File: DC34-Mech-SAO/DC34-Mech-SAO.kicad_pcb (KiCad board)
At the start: 2 copper layers, 27.9 x 38 mm, 20 parts, among them J1 Conn_01x06_Male, J2 Conn_01x03_Male, U1 ATtiny816-M

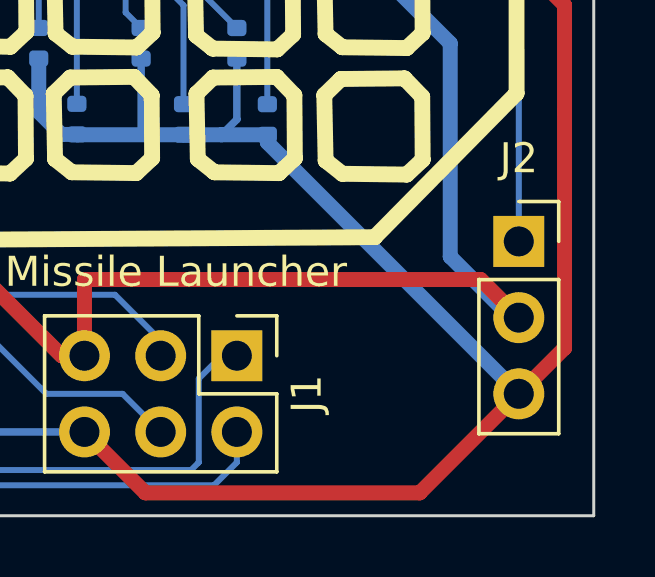
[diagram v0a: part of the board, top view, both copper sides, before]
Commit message: Added silkscreen.
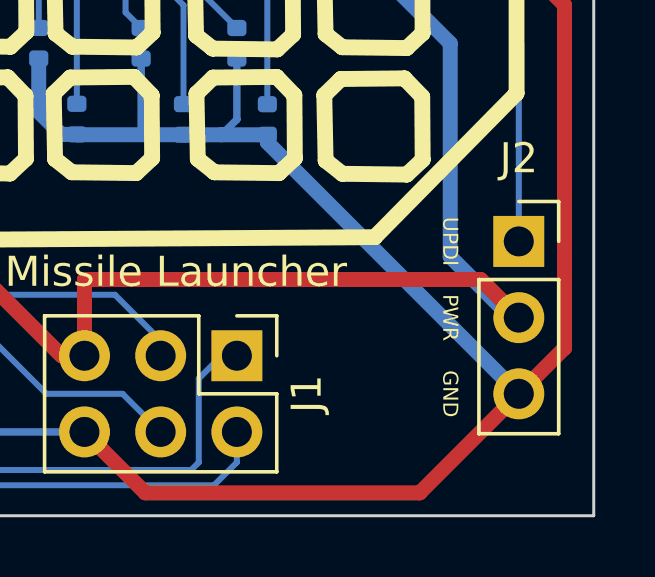
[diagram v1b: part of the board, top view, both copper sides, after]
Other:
- board text added: "Designed by CPEC in Arizona"
- board text added: "GND"
- board text added: "Manufactured in China"
- board text added: "Mech Fighters SAO Rev 1"
- board text added: "PWR"
- board text added: "UPDI"
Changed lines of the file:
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@@
   (gr_line (start 149.691132 72.230133) (end 149.691132 72.230133) (layer "F.SilkS") (width 0.529166))
   (gr_rect (start 130.852 62.06) (end 158.708 100.076) (layer "Edge.Cuts") (width 0.1) (fill none))
+  (gr_text "Manufactured in China" (at 144.526 91.44) (layer "B.SilkS")
+    (effects (font (size 1 1) (thickness 0.15)) (justify mirror))
+  )
+  (gr_text "Mech Fighters SAO Rev 1" (at 144.78 80.518) (layer "B.SilkS")
+    (effects (font (size 1 1) (thickness 0.15)) (justify mirror))
+  )
+  (gr_text "Designed by CPEC in Arizona" (at 143.256 89.916) (layer "B.SilkS")
+    (effects (font (size 1 1) (thickness 0.15)) (justify mirror))
+  )
+  (gr_text "PWR" (at 153.924 93.472 270) (layer "F.SilkS")
+    (effects (font (size 0.5 0.5) (thickness 0.07)))
+  )
+  (gr_text "UPDI" (at 153.924 90.932 270) (layer "F.SilkS")
+    (effects (font (size 0.5 0.5) (thickness 0.07)))
+  )
   (gr_text "Missile Launcher" (at 144.78 91.948) (layer "F.SilkS")
     (effects (font (size 1 1) (thickness 0.15)))
   )
+  (gr_text "GND" (at 153.924 96.012 270) (layer "F.SilkS")
+    (effects (font (size 0.5 0.5) (thickness 0.07)))
+  )
   (via (at 134.874 88.646) (size 0.8) (drill 0.4) (layers "F.Cu" "B.Cu") (free) (net 0))
